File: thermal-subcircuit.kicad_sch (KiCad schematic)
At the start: 16 parts, among them Q1 SQ3461EV, U2 TS5A3159-Q1, U3 TLV1805-Q1DBV

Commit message: work
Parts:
- renumbered R1 to R15, R2 to R16, R3 to R17, R4 to R18, R5 to R19, R6 to R20, R7 to R21, R251 to R22, U2 to U1, U3 to U2

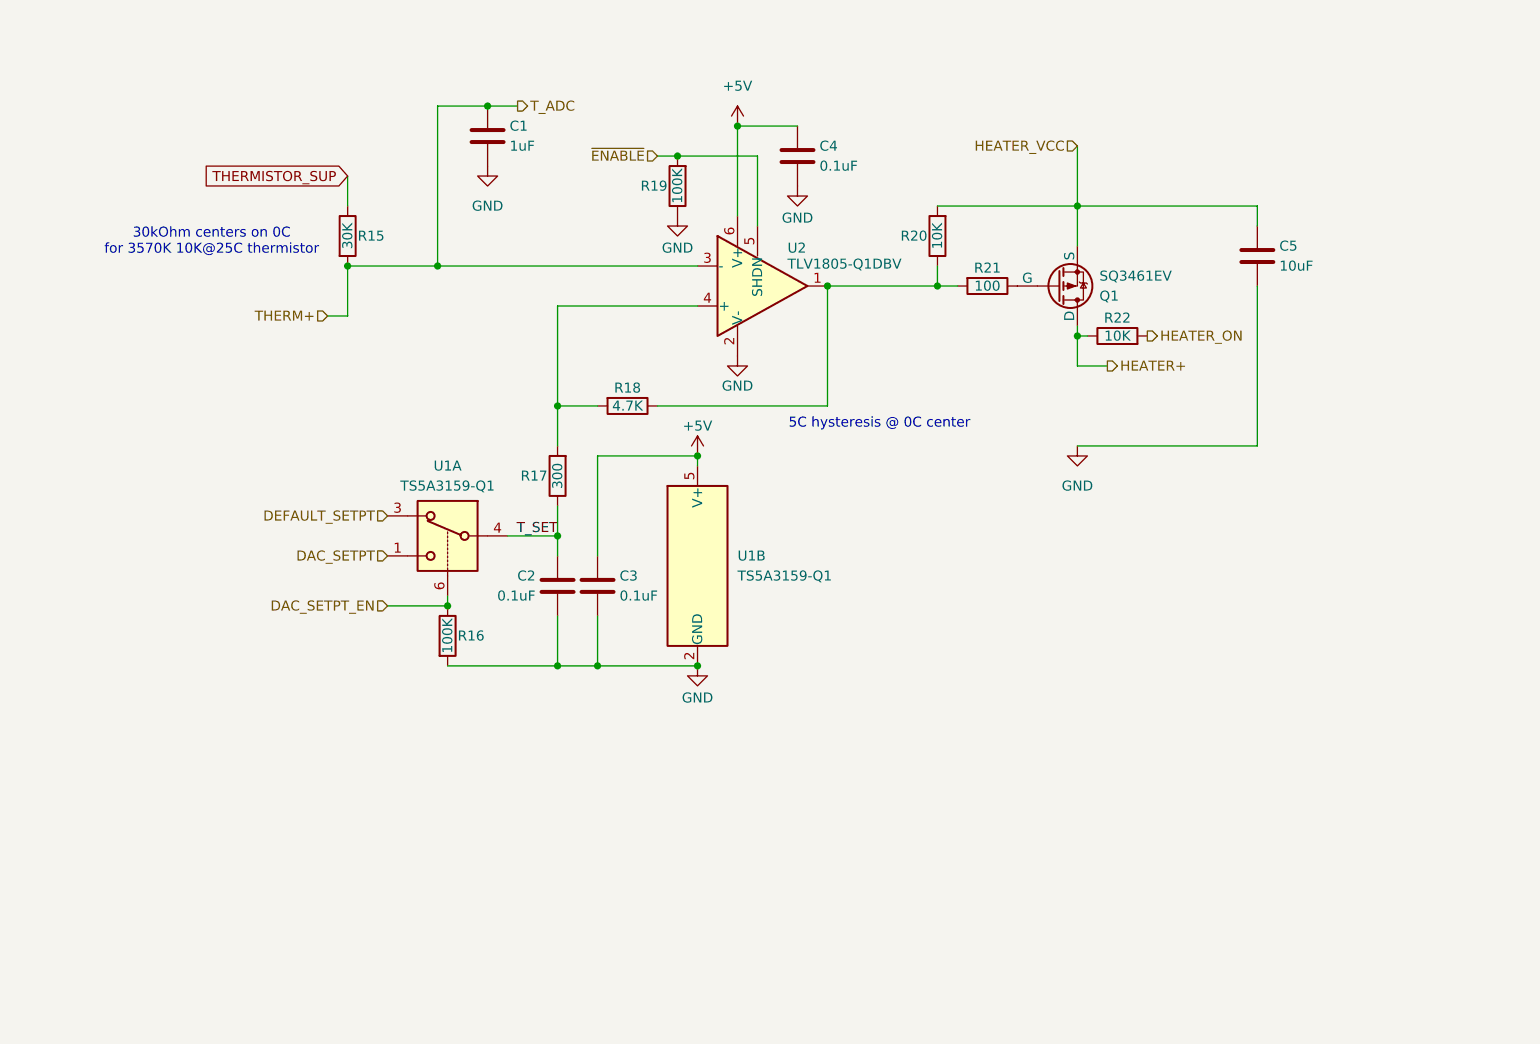
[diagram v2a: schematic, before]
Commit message: consolidate heaters
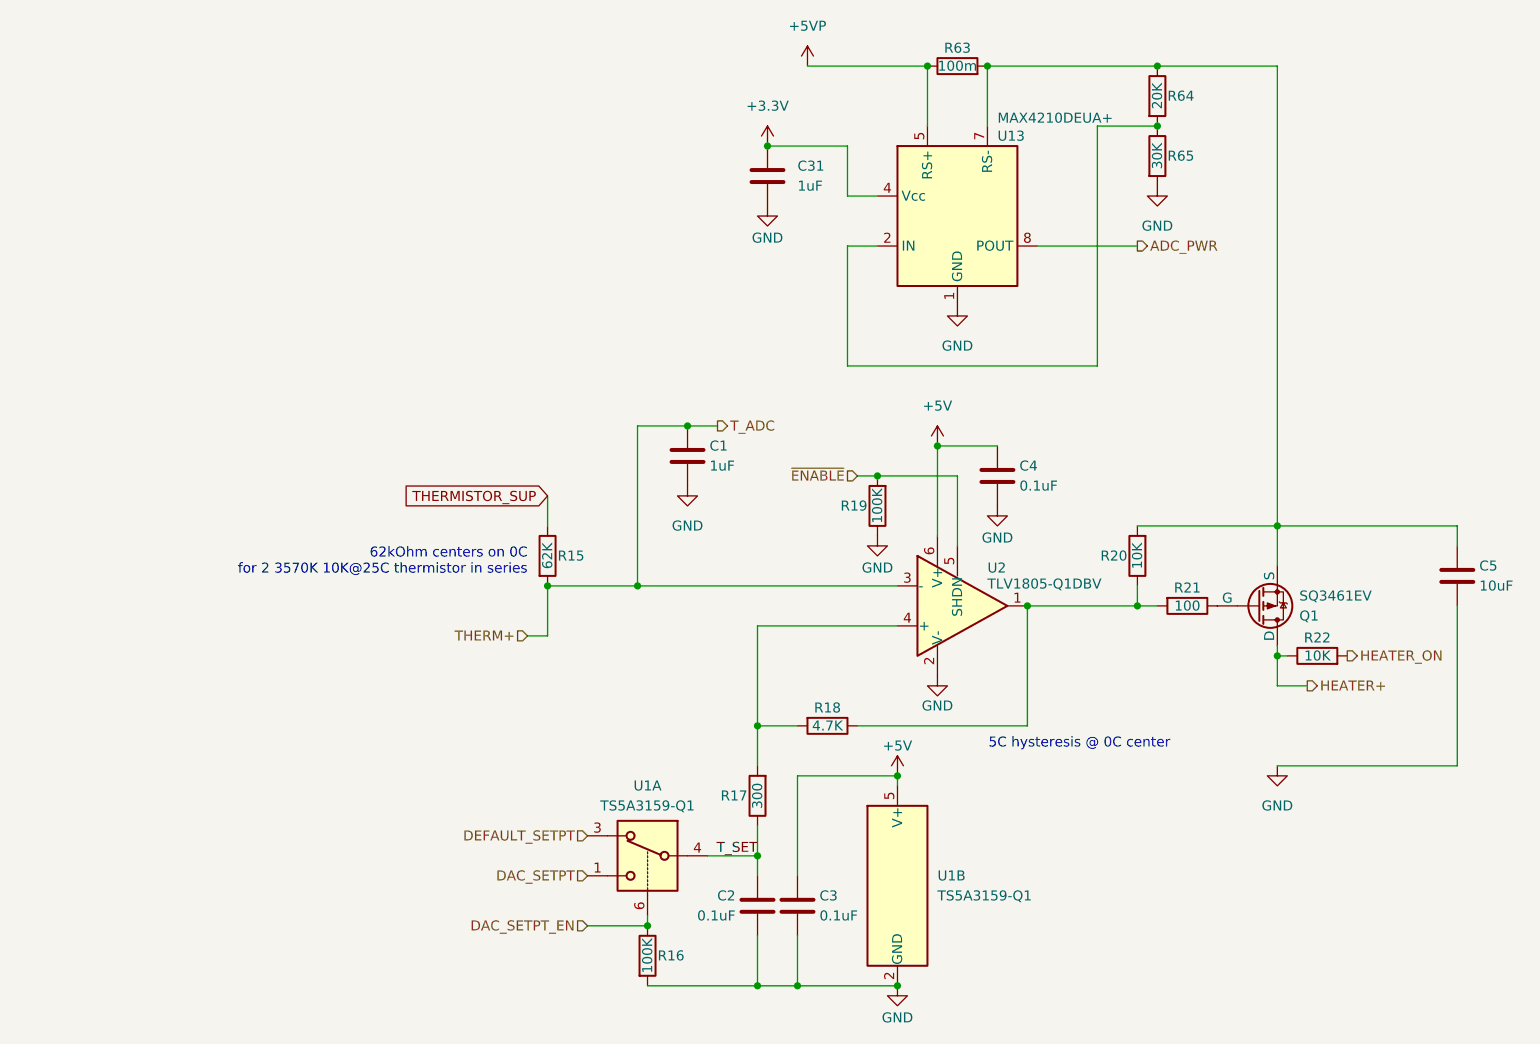
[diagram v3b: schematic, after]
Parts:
- added C31: 1uF, symbol Device:C
- added R63: 100m, symbol Device:R
- added R64: 20K, symbol Device:R
- added R65: 30K, symbol Device:R
- added U13: MAX4210DEUA+, symbol femta-control-custom:MAX4210
- R15: value 30K -> 62K
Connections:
- net GND: now also C31.2, R65.2, U13.1 (GND)
- net HEATER_VCC: no longer names the net of C5.1, Q1.4 (S), R20.2
- net HEATER_VCC: now also R63.2, R64.1, U13.7 (RS-)
- new net: R64.2, R65.1, U13.2 (IN)
- new net: U13.3 (NC), U13.6 (NC)
- new net +3.3V: C31.1, U13.4 (Vcc)
- new net +5VP: R63.1, U13.5 (RS+)
- new net ADC_PWR: U13.8 (POUT)
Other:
- note added: "62kOhm centers on 0C for 2 3570K 10K@25C thermistor in series"
- note removed: "30kOhm centers on 0C for 3570K 10K@25C thermistor"
- moved on the sheet: C1, C2, C3, C4, C5, Q1, R15, R16, R17, R18, R19, R20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

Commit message: work
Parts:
- added NT1: HEATER TRACE, symbol Device:NetTie_2
- added R30: 30K, symbol Device:R
- added TH1: NTCS0805E3103HMT, symbol Device:Thermistor
- R22: value 10K -> 20K
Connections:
- net GND: now also NT1.1, R30.2, TH1.2
- net HEATER_ON: now also R30.1
- net HEATER+: no longer names the net of Q1.1 (D), Q1.2 (D), Q1.5 (D), Q1.6 (D), R22.1
- net HEATER+: now also NT1.2
- net THERM+ renamed T_ADC
- net T_ADC: now also TH1.1

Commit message: lots and lots and lots of work
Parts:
- R64: value 20K -> 51K
- R65: value 30K -> 13K
- U13: value MAX4210DEUA+ -> MAX4210FEUA+
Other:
- note added: "V(pout) = 0.832*POUT, 3.966W max power"
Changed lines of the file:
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@@
+		)
+	)
+	(text "V(pout) = 0.832*POUT, 3.966W max power"
+		(exclude_from_sim no)
+		(at 134.366 84.328 0)
+		(effects
+			(font
+				(size 1.27 1.27)
+			)
 		)
 	)
@@
 			)
 		)
-		(property "Value" "20K"
+		(property "Value" "51K"
 			(at 156.21 48.26 90)
 			(effects
@@
 			)
 		)
-		(property "Value" "MAX4210DEUA+"
+		(property "Value" "MAX4210FEUA+"
 			(at 135.89 51.054 0)
 			(do_not_autoplace yes)
@@
 			)
 		)
-		(property "Value" "30K"
+		(property "Value" "13K"
 			(at 156.21 55.88 90)
 			(effects

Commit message: 540 COMPONENTS I AM LOSING MY MINDDDDDD
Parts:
- added TH7: NTCS0805E3103HMT, Resistor_SMD:R_0805_2012Metric, symbol Device:Thermistor
- TH1: footprint (none) -> Resistor_SMD:R_0805_2012Metric
- renumbered C1 to C78, C2 to C79, C31 to C80, C3 to C81, C4 to C82, C5 to C83, Q1 to Q19, R15 to R114, R16 to R115, R17 to R116, R18 to R117, R19 to R118, R63 to R119, R20 to R120, R64 to R121, R65 to R122, R21 to R123, R22 to R124, R30 to R125, U1 to U76, U13 to U77, U2 to U78
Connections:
- net T_ADC: now also TH7.1; no longer TH1.1
- new net: TH1.1, TH7.2
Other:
- moved on the sheet: R114, TH1

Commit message: schematic finished milestone
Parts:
- renumbered C81 to C100, C82 to C101, C83 to C102, C78 to C97, C79 to C98, C80 to C99, R114 to R123, R115 to R124, R116 to R125, R117 to R126, R118 to R127, R119 to R128, R120 to R129, R121 to R130, R122 to R131, R123 to R132, R124 to R133, R125 to R134, TH7 to TH1, TH1 to TH2
